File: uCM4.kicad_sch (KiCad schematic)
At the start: 65 parts, among them J1 UART, J10 Conn_01x04, J11 Conn_02x06_Odd_Even, J2 Micro_SD_Card_Det, J3 I2C1, J4 USB_B_Micro, J5 DummyJ, J6 DummyJ, J7 SolderJumper_2_Open, J8 Camera 0, J9 Camera 1, SW1 SW_DIP_x01, SW2 SW_DIP_x01, SW3 SW_Push, SW4 SW_Push, U1 BNO055, U18 RT9742GGJ5, U2 SN74LVC1G07DBVR, U3 TPD4EUSB30DQAR, U4 TPS61022, U5 BME690

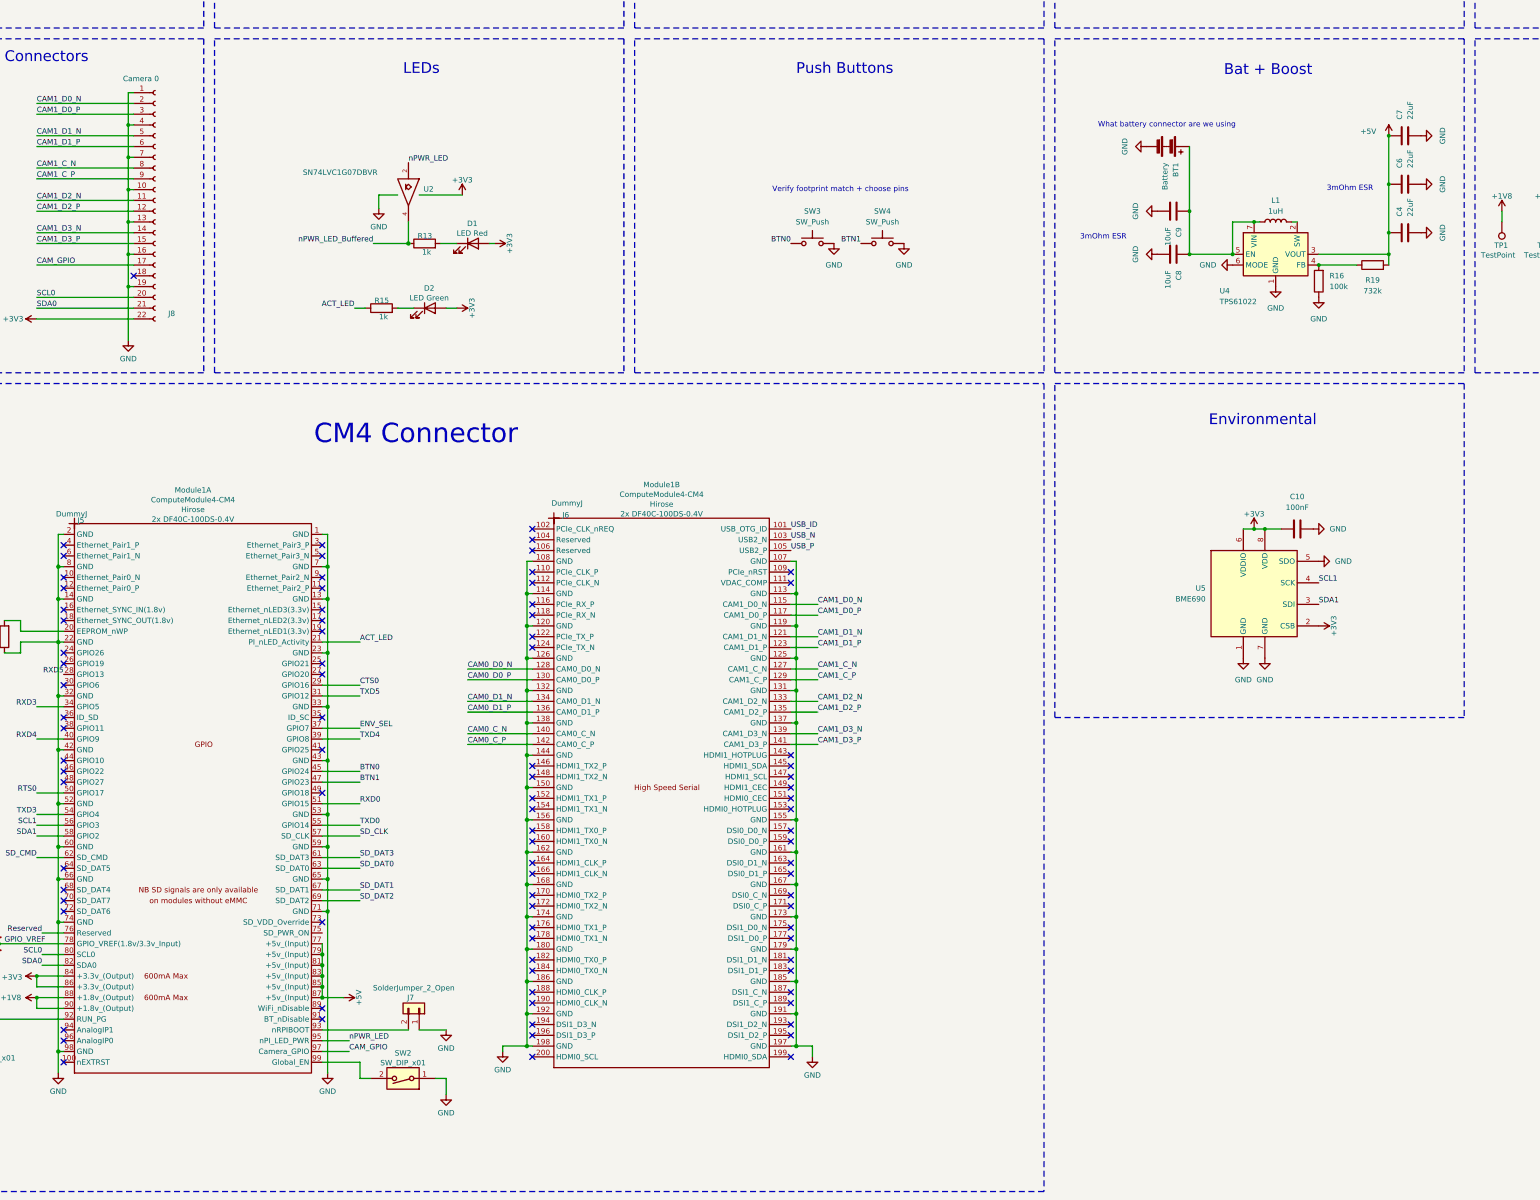
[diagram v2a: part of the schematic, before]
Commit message: Changing connectors and arranging PCB.
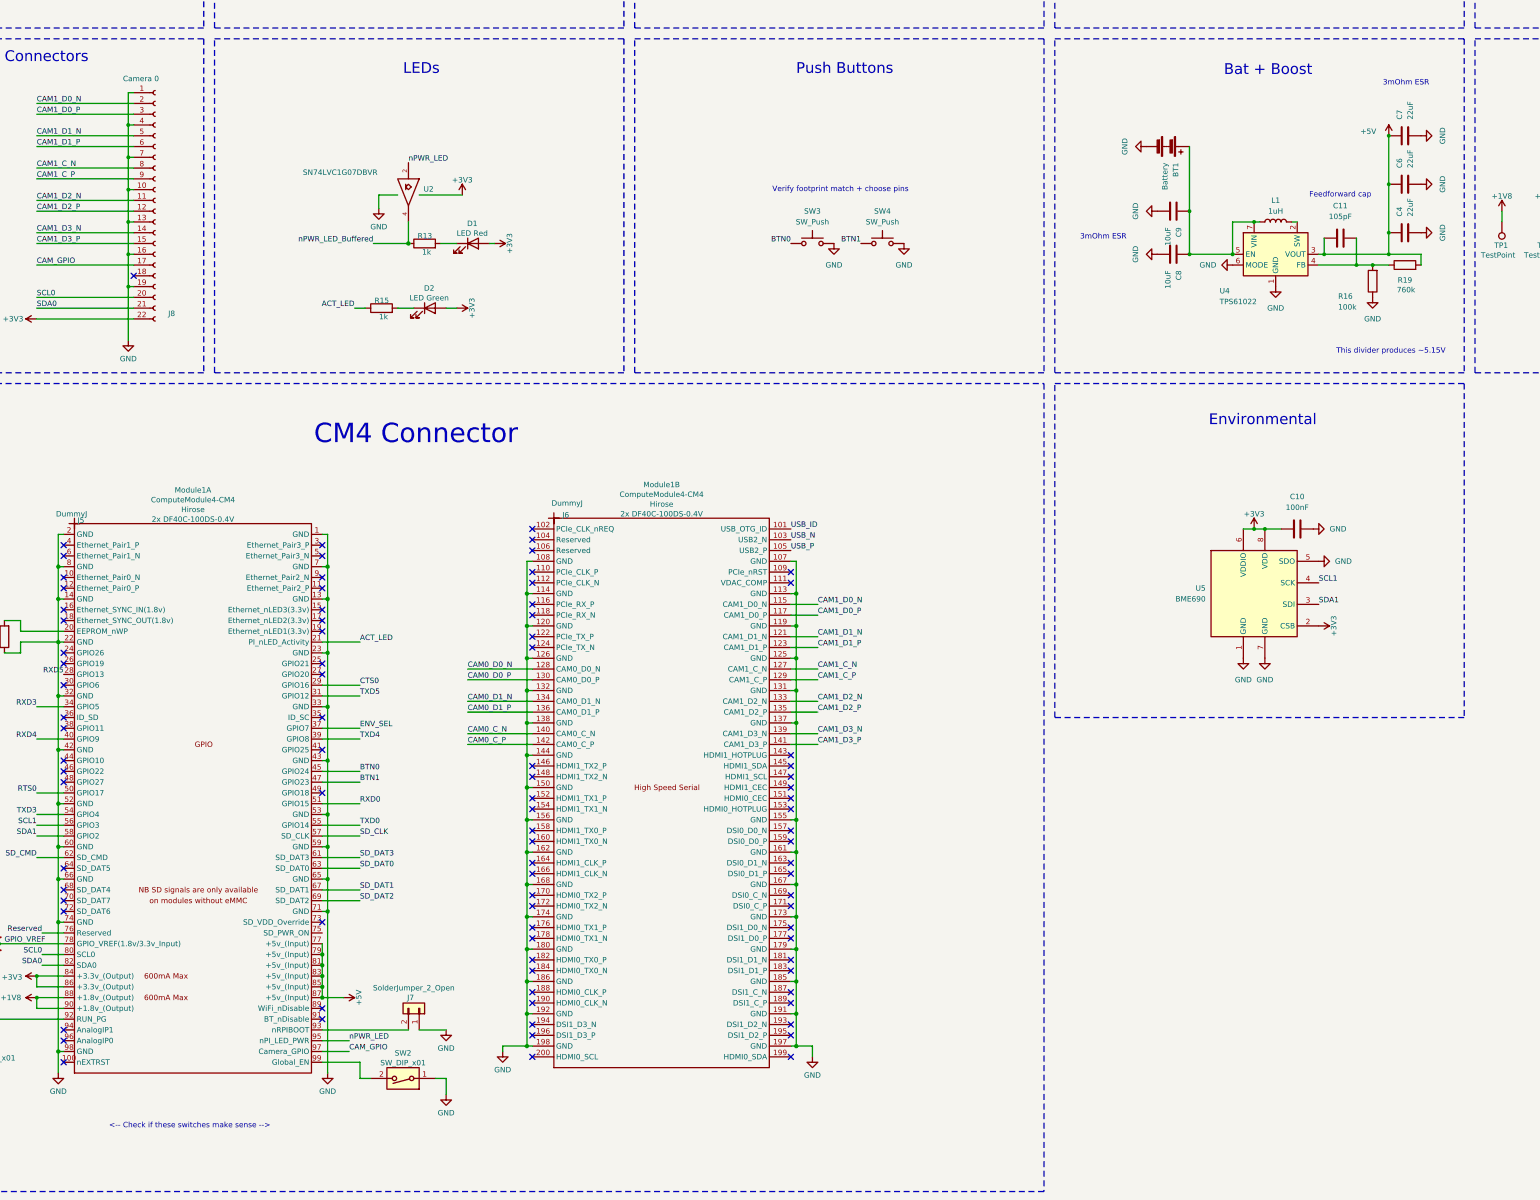
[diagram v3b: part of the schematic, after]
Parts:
- added C11: 105pF, Capacitor_SMD:C_0603_1608Metric, symbol Device:C
- BT1: footprint Connector_Molex:Molex_SL_171971-0002_1x02_P2.54mm_Vertical -> Connector_JST:JST_PH_B2B-PH-K_1x02_P2.00mm_Vertical
- R19: value 732k -> 760k
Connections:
- net +5V: now also C11.1
- net at R16.2, R19.1, U4.4 (FB): now also C11.2
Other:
- note added: "<-- Check if these switches make sense -->"
- note added: "Feedforward cap"
- note added: "This divider produces ~5.15V"
- note removed: "What battery connector are we using"
- moved on the sheet: R16, R19
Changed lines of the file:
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@@
 	(text "3mOhm ESR"
 		(exclude_from_sim no)
-		(at 383.286 134.366 0)
+		(at 396.494 109.474 0)
 		(effects
 			(font
@@
 		)
 	)
-	(text "What battery connector are we using"
-		(exclude_from_sim no)
-		(at 340.106 119.38 0)
-		(effects
-			(font
-				(size 1.27 1.27)
-				(color 255 0 2 1)
-			)
-		)
-	)
 	(text "CM4Lite SDCARD I/F"
 		(exclude_from_sim no)
@@
 		)
 	)
+	(text "This divider produces ~5.15V"
+		(exclude_from_sim no)
+		(at 392.938 172.72 0)
+		(effects
+			(font
+				(size 1.27 1.27)
+			)
+		)
+	)
 	(text "Environmental"
 		(exclude_from_sim no)
@@
 		)
 	)
+	(text "<-- Check if these switches make sense -->"
+		(exclude_from_sim no)
+		(at 109.728 355.346 0)
+		(effects
+			(font
+				(size 1.27 1.27)
+				(color 255 0 6 1)
+			)
+		)
+	)
 	(text "Camera Connectors"
 		(exclude_from_sim no)
@@
 		)
 	)
+	(text "Feedforward cap"
+		(exclude_from_sim no)
+		(at 381 135.89 0)
+		(effects
+			(font
+				(size 1.27 1.27)
+			)
+		)
+	)
 	(text "Why is N to + and P to - ?"
 		(exclude_from_sim no)
@@
 	)
 	(junction
+		(at 388.62 152.4)
+		(diameter 0)
+		(color 0 0 0 0)
+	)
+	(junction
 		(at 78.74 266.7)
 		(diameter 1.016)
@@
 	)
 	(junction
-		(at 375.92 152.4)
-		(diameter 0)
-		(color 0 0 0 0)
-	)
-	(junction
 		(at 142.24 256.54)
 		(diameter 1.016)
@@
 	)
 	(junction
+		(at 377.19 149.86)
+		(diameter 0)
+		(color 0 0 0 0)
+	)
+	(junction
 		(at 252.73 336.55)
 		(diameter 1.016)
@@
 		(color 0 0 0 0)
 	)
+	(junction
+		(at 384.81 152.4)
+		(diameter 0)
+		(color 0 0 0 0)
+	)
 	(no_connect
 		(at 80.01 335.28)
@@
 	(wire
 		(pts
+			(xy 384.81 146.05) (xy 384.81 152.4)
+		)
+		(stroke
+			(width 0)
+			(type default)
+		)
+	)
+	(wire
+		(pts
 			(xy 73.66 116.84) (xy 96.52 116.84)
 		)
@@
 	(wire
 		(pts
+			(xy 377.19 146.05) (xy 377.19 149.86)
+		)
+		(stroke
+			(width 0)
+			(type default)
+		)
+	)
+	(wire
+		(pts
 			(xy 73.66 292.1) (xy 80.01 292.1)
 		)
@@
 	(wire
 		(pts
-			(xy 375.92 149.86) (xy 392.43 149.86)
+			(xy 375.92 149.86) (xy 377.19 149.86)
 		)
 		(stroke
@@
 	(wire
 		(pts
-			(xy 392.43 149.86) (xy 392.43 152.4)
+			(xy 400.05 149.86) (xy 400.05 152.4)
 		)
 		(stroke
@@
 	(wire
 		(pts
+			(xy 392.43 152.4) (xy 388.62 152.4)
+		)
+		(stroke
+			(width 0)
+			(type default)
+		)
+	)
+	(wire
+		(pts
 			(xy 363.22 214.63) (xy 367.03 214.63)
 		)
@@
 	(wire
 		(pts
+			(xy 388.62 152.4) (xy 384.81 152.4)
+		)
+		(stroke
+			(width 0)
+			(type default)
+		)
+	)
+	(wire
+		(pts
 			(xy 294.64 68.58) (xy 297.18 68.58)
 		)
@@
 	(wire
 		(pts
-			(xy 384.81 152.4) (xy 375.92 152.4)
-		)
-		(stroke
-			(width 0)
-			(type default)
-		)
-	)
-	(wire
-		(pts
 			(xy 189.23 283.21) (xy 189.23 290.83)
 		)
@@
 	(wire
 		(pts
+			(xy 377.19 149.86) (xy 392.43 149.86)
+		)
+		(stroke
+			(width 0)
+			(type default)
+		)
+	)
+	(wire
+		(pts
 			(xy 46.99 142.24) (xy 46.99 149.86)
 		)
@@
 	(wire
 		(pts
+			(xy 375.92 152.4) (xy 384.81 152.4)
+		)
+		(stroke
+			(width 0)
+			(type default)
+		)
+	)
+	(wire
+		(pts
 			(xy 34.29 46.99) (xy 40.64 46.99)
 		)
@@
 	(wire
 		(pts
+			(xy 400.05 149.86) (xy 392.43 149.86)
+		)
+		(stroke
+			(width 0)
+			(type default)
+		)
+	)
+	(wire
+		(pts
 			(xy 78.74 215.9) (xy 78.74 223.52)
 		)
@@
 		(lib_name "GND_4")
 		(lib_id "power:GND")
-		(at 375.92 160.02 0)
+		(at 388.62 160.02 0)
 		(unit 1)
 		(exclude_from_sim no)
@@
 		(fields_autoplaced yes)
 		(property "Reference" "#PWR031"
-			(at 375.92 166.37 0)
+			(at 388.62 166.37 0)
 			(effects
 				(font
@@
 		)
 		(property "Value" "GND"
-			(at 375.92 165.1 0)
+			(at 388.62 165.1 0)
 			(effects
 				(font
@@
 		)
 		(property "Footprint" ""
-			(at 375.92 160.02 0)
+			(at 388.62 160.02 0)
 			(effects
 				(font
@@
 		)
 		(property "Datasheet" ""
-			(at 375.92 160.02 0)
+			(at 388.62 160.02 0)
 			(effects
 				(font
@@
 		)
 		(property "Description" "Power symbol creates a global label with name \"GND\" , ground"
-			(at 375.92 160.02 0)
+			(at 388.62 160.02 0)
 			(effects
 				(font
@@
 	(symbol
 		(lib_id "Device:R")
-		(at 375.92 156.21 180)
+		(at 388.62 156.21 180)
 		(unit 1)
 		(exclude_from_sim no)
@@
 		(on_board yes)
 		(dnp no)
-		(fields_autoplaced yes)
 		(property "Reference" "R16"
-			(at 378.46 154.9399 0)
+			(at 380.492 159.766 0)
 			(effects
 				(font
@@
 		)
 		(property "Value" "100k"
-			(at 378.46 157.4799 0)
+			(at 380.492 162.306 0)
 			(effects
 				(font
@@
 		)
 		(property "Footprint" "Resistor_SMD:R_0603_1608Metric"
-			(at 377.698 156.21 90)
+			(at 390.398 156.21 90)
 			(effects
 				(font
@@
 		)
 		(property "Datasheet" "~"
-			(at 375.92 156.21 0)
+			(at 388.62 156.21 0)
 			(effects
 				(font
@@
 		)
 		(property "Description" "Resistor"
-			(at 375.92 156.21 0)
+			(at 388.62 156.21 0)
 			(effects
 				(font
@@
 	(symbol
 		(lib_id "Device:C")
+		(at 381 146.05 90)
+		(unit 1)
+		(exclude_from_sim no)
+		(in_bom yes)
+		(on_board yes)
+		(dnp no)
+		(fields_autoplaced yes)
+		(property "Reference" "C11"
+			(at 381 138.43 90)
+			(effects
+				(font
+					(size 1.27 1.27)
+				)
+			)
+		)
+		(property "Value" "105pF"
+			(at 381 140.97 90)
+			(effects
+				(font
+					(size 1.27 1.27)
+				)
+			)
+		)
+		(property "Footprint" "Capacitor_SMD:C_0603_1608Metric"
+			(at 384.81 145.0848 0)
+			(effects
+				(font
+					(size 1.27 1.27)
+				)
+				(hide yes)
+			)
+		)
+		(property "Datasheet" "~"
+			(at 381 146.05 0)
+			(effects
+				(font
+					(size 1.27 1.27)
+				)
+				(hide yes)
+			)
+		)
+		(property "Description" "Unpolarized capacitor"
+			(at 381 146.05 0)
+			(effects
+				(font
+					(size 1.27 1.27)
+				)
+				(hide yes)
+			)
+		)
+		(pin "2"
+		)
+		(pin "1"
+		)
+		(instances
+			(project ""
+				(path "/ab308ddb-f5b4-4376-8062-4d719b3e690f"
+					(reference "C11")
+					(unit 1)
+				)
+			)
+		)
+	)
+	(symbol
+		(lib_id "Device:C")
 		(at 358.14 40.64 90)
 		(unit 1)
@@
 	(symbol
 		(lib_id "Device:R")
-		(at 388.62 152.4 90)
+		(at 396.24 152.4 90)
 		(unit 1)
 		(exclude_from_sim no)
@@
 		(dnp no)
 		(property "Reference" "R19"
-			(at 388.62 155.956 90)
+			(at 396.24 155.956 90)
 			(effects
 				(font
@@
 			)
 		)
-		(property "Value" "732k"
-			(at 388.62 158.496 90)
+		(property "Value" "760k"
+			(at 396.494 158.242 90)
 			(effects
 				(font
@@
 		)
 		(property "Footprint" "Resistor_SMD:R_0603_1608Metric"
-			(at 388.62 154.178 90)
+			(at 396.24 154.178 90)
 			(effects
 				(font
@@
 		)
 		(property "Datasheet" "~"
-			(at 388.62 152.4 0)
+			(at 396.24 152.4 0)
 			(effects
 				(font
@@
 		)
 		(property "Description" "Resistor"
-			(at 388.62 152.4 0)
+			(at 396.24 152.4 0)
 			(effects
 				(font
@@
 			)
 		)
-		(property "Footprint" "Connector_Molex:Molex_SL_171971-0002_1x02_P2.54mm_Vertical"
+		(property "Footprint" "Connector_JST:JST_PH_B2B-PH-K_1x02_P2.00mm_Vertical"
 			(at 341.884 124.46 90)
 			(effects

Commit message: Changing models & some initial routing
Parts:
- removed J1: UART, Connector_PinHeader_2.54mm:PinHeader_1x06_P2.54mm_Vertical, symbol Connector_Generic:Conn_01x06
- removed J10: Conn_01x04, Connector_PinHeader_2.54mm:PinHeader_1x04_P2.54mm_Vertical, symbol Connector_Generic:Conn_01x04
- removed J11: Conn_02x06_Odd_Even, Connector_PinHeader_2.54mm:PinHeader_2x06_P2.54mm_Vertical, symbol Connector_Generic:Conn_02x06_Odd_Even
- removed J3: I2C1, Connector_PinHeader_2.54mm:PinHeader_1x04_P2.54mm_Vertical, symbol Connector_Generic:Conn_01x04
- removed R5, R8, R9: 0, Resistor_SMD:R_0603_1608Metric_Pad0.98x0.95mm_HandSolder, symbol Device:R
- added J1: Conn_02x07_Odd_Even, Connector_PinHeader_2.54mm:PinHeader_2x07_P2.54mm_Vertical, symbol Connector_Generic:Conn_02x07_Odd_Even
- added J12: Conn_02x08_Odd_Even, Connector_PinHeader_2.54mm:PinHeader_2x08_P2.54mm_Vertical_SMD, symbol Connector_Generic:Conn_02x08_Odd_Even
- added R20, R21, R22: 0, Resistor_SMD:R_0603_1608Metric_Pad0.98x0.95mm_HandSolder, symbol Device:R
- added TP10: TestPoint, TestPoint:TestPoint_Pad_D1.0mm, symbol Connector:TestPoint
- BT1: footprint Connector_JST:JST_PH_B2B-PH-K_1x02_P2.00mm_Vertical -> Connector_JST:JST_PH_S2B-PH-K_1x02_P2.00mm_Horizontal
- J7: footprint Connector_PinHeader_2.54mm:PinHeader_1x02_P2.54mm_Vertical -> Jumper:SolderJumper-2_P1.3mm_Open_RoundedPad1.0x1.5mm
- SW3, SW4: footprint Button_Switch_SMD:SW_Push_1P1T_NO_E-Switch_TL3301NxxxxxG -> KiCAD_Randoms:PTS840_PM_SMTR_LFS
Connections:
- net +3V3: now also R20.1, R21.1, R22.1
- net CTS0: now also J12.3 (Pin_3)
- net GND: now also J1.3 (Pin_3), J1.4 (Pin_4), J12.1 (Pin_1), J12.14 (Pin_14), J12.6 (Pin_6)
- net GPS_EN_1: now also J1.1 (Pin_1)
- net GPS_EN_2: now also J1.2 (Pin_2)
- net GPS_PPS_1: now also J1.11 (Pin_11), J1.12 (Pin_12)
- net RTS0: now also J12.11 (Pin_11)
- net RXD0: now also J12.9 (Pin_9)
- net RXD3: now also J1.7 (Pin_7)
- net RXD4: now also J1.8 (Pin_8)
- net SCL0: now also J12.2 (Pin_2)
- net SCL1: now also J12.10 (Pin_10)
- net SDA0: now also J12.4 (Pin_4)
- net SDA1: now also J12.12 (Pin_12)
- net TXD0: now also J12.7 (Pin_7)
- net TXD3: now also J1.5 (Pin_5)
- net TXD4: now also J1.6 (Pin_6)
- net BAT_IN: now reaches BT1.1 (+), C8.1, C9.1, L1.1, U4.5 (EN), U4.7 (VIN)
- net BAT_IN: now also TP10.1
- net at R10.1: now also J1.10 (Pin_10)
- net at R11.2: now also J1.9 (Pin_9)
- new net: J12.8 (Pin_8), R22.2
- new net: J12.5 (Pin_5), R20.2
- new net: J12.16 (Pin_16), R21.2
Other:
- note added: "This needs to be changed now"

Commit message: Added STEMMA connector and some comments
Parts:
- added J3: Conn_01x04, Connector_JST:JST_PH_B4B-PH-K_1x04_P2.00mm_Vertical, symbol Connector_Generic:Conn_01x04
- added R5: 0, Resistor_SMD:R_0603_1608Metric_Pad0.98x0.95mm_HandSolder, symbol Device:R
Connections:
- net +3V3: now also R5.1
- net GND: now also J3.1 (Pin_1)
- net SCL0: now also J3.4 (Pin_4)
- net SDA0: now also J3.3 (Pin_3)
- new net: J3.2 (Pin_2), R5.2
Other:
- note added: "Fuel gauge? External i2c environmental sensor SPI output Remove all parts from bottom of board Add at least 2 user LEDs RPi boot debug jumper (EMCC) Check HaLow compat if possible"
- note added: "Stemma/QUIIC Connector for external sensors"

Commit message: Added fuel gauge + USB C + some other things
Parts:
- removed J4: USB_B_Micro, Special:U254-05XX-4BH81, symbol Connector:USB_B_Micro
- removed R21, R22: 0, Resistor_SMD:R_0603_1608Metric_Pad0.98x0.95mm_HandSolder, symbol Device:R
- added C13: 100nF, Capacitor_SMD:C_0603_1608Metric, symbol Device:C
- added D3, D4: LED, symbol Device:LED
- added IC1: MAX17048G+, CM4:SON50P200X200X80-9N-D, symbol CM4IO:MAX17048G+
- added J10: USB_C_Receptacle, Connector_USB:USB_C_Receptacle_Amphenol_12401610E4-2A, symbol Connector:USB_C_Receptacle
- added J11: SolderJumper_2_Open, Connector_PinHeader_2.54mm:PinHeader_1x02_P2.54mm_Vertical_SMD_Pin1Left, symbol Connector_Generic:Conn_01x02
- added J4: Conn_01x04, Connector_JST:JST_PH_B4B-PH-K_1x04_P2.00mm_Vertical, symbol Connector_Generic:Conn_01x04
- added R23: 0, Resistor_SMD:R_0603_1608Metric_Pad0.98x0.95mm_HandSolder, symbol Device:R
- added R8, R9: 5.1k, Resistor_SMD:R_0402_1005Metric, symbol Device:R
- J7: footprint Jumper:SolderJumper-2_P1.3mm_Open_RoundedPad1.0x1.5mm -> Connector_PinHeader_2.54mm:PinHeader_1x02_P2.54mm_Vertical_SMD_Pin1Left
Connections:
- net +3V3: now also R23.1
- net BAT_IN: now also C13.1, IC1.2 (CELL), IC1.3 (VDD)
- net GND: now also C13.2, IC1.1 (CTG), IC1.4 (GND), IC1.6 (QSTRT), IC1.9 (EP), J10.A1 (GND), J10.A12 (GND), J10.B1 (GND), J10.B12 (GND), J10.S1 (SHIELD), J11.1 (Pin_1), J4.1 (Pin_1), R8.2, R9.2; no longer J12.14 (Pin_14), J12.6 (Pin_6)
- net SCL0: now also IC1.7 (SCL); no longer J12.2 (Pin_2)
- net SCL1: now also J4.4 (Pin_4); no longer J12.10 (Pin_10)
- net SDA0: now also IC1.8 (SDA); no longer J12.4 (Pin_4)
- net SDA1: now also J4.3 (Pin_3); no longer J12.12 (Pin_12)
- net USB_ID: no longer Module1.101 (USB_OTG_ID)
- net USB_N: now also J10.A7 (D-), J10.B7 (D-)
- net USB_P: now also J10.A6 (D+), J10.B6 (D+)
- net BAT_ALERT: now reaches Module1.41 (GPIO25)
- net BAT_ALERT: now also IC1.5 (~{ALRT})
- new net: J11.2 (Pin_2), Module1.101 (USB_OTG_ID)
- new net: J10.A5 (CC1), R8.1
- new net: J4.2 (Pin_2), R23.2
- new net: J10.B5 (CC2), R9.1
- new net VBUS: J10.A4 (VBUS), J10.A9 (VBUS), J10.B4 (VBUS), J10.B9 (VBUS)
- no-connect marks 99 -> 108
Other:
- note added: "Add SPI here"
- note added: "Bat_Mon"
- note added: "Controls host mode"
- note added: "Handle VBUS input to power path"
- note added: "SPI output Remove all parts from bottom of board Check HaLow compat if possible"
- note added: "USER LEDS"
- note removed: "Fuel gauge? External i2c environmental sensor SPI output Remove all parts from bottom of board Add at least 2 user LEDs RPi boot debug jumper (EMCC) Check HaLow compat if possible"
- note removed: "Why is N to + and P to - ?"
- moved on the sheet: J12, J3, R20, R5
